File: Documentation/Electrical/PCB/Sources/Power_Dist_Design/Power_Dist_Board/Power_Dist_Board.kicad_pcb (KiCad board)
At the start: 2 copper layers, 145 x 85 mm, 66 parts, among them J1 Battery Connector, J10 GND_Bridge_3, J2 +5V, J3 +5V, J4 +3.3V, J5 +3.3V, J6 GND, J7 GND, J8 GND_Bridge_1, J9 GND_Bridge_2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

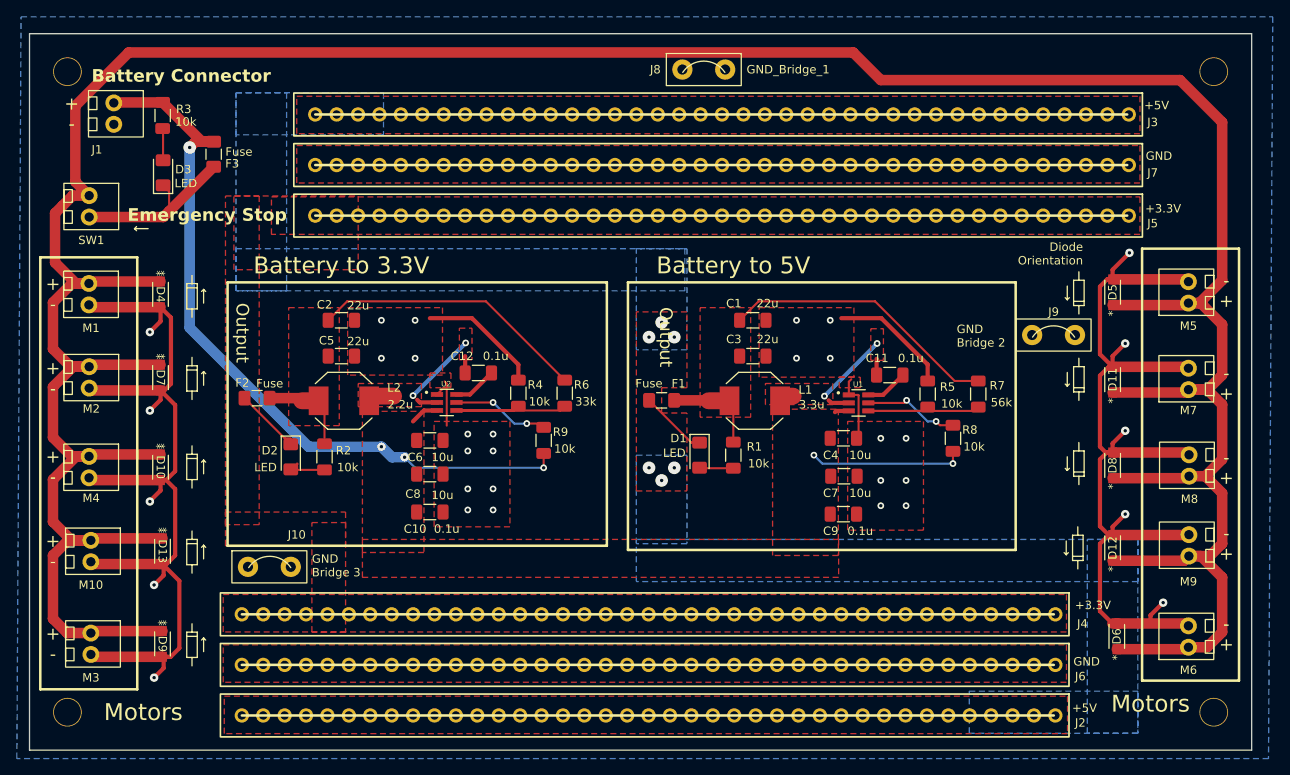
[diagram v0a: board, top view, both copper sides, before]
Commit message: added 3d models to pcb
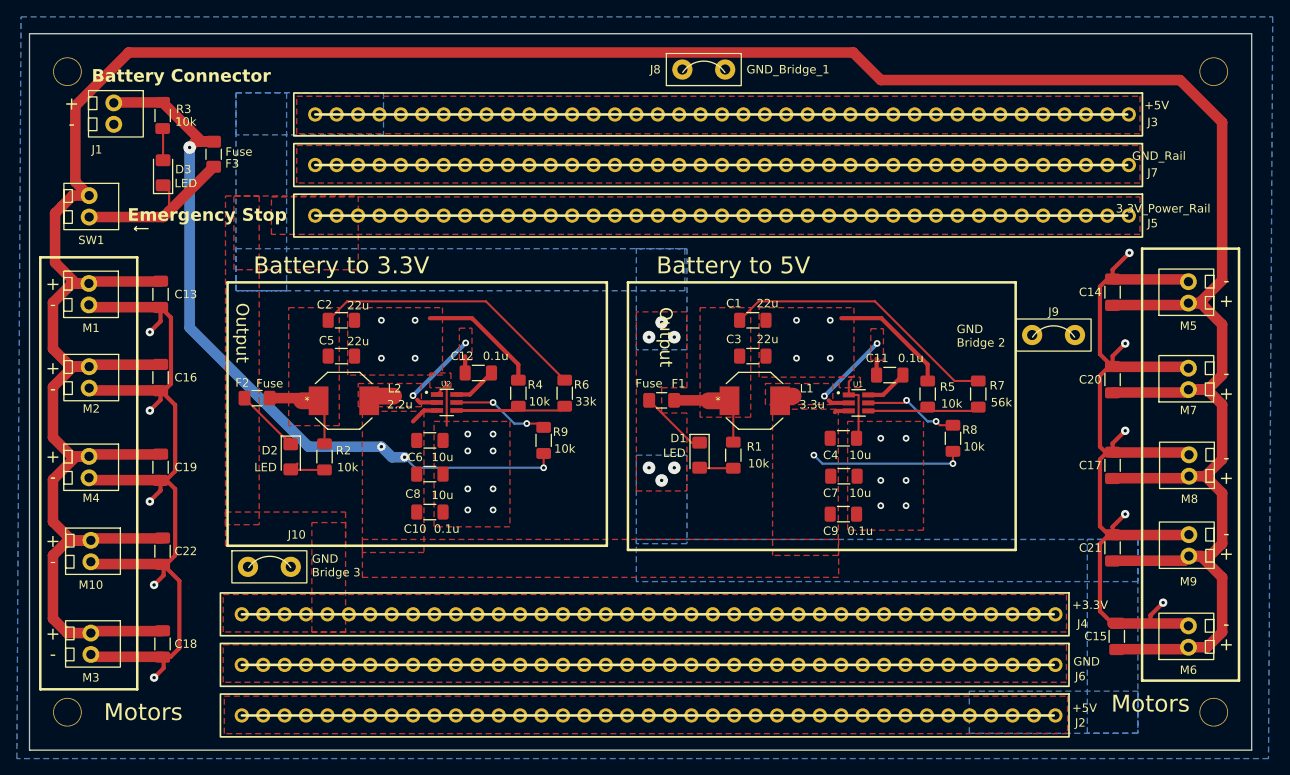
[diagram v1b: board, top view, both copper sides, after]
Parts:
- C13: renamed from D4; value D -> 0.1u; footprint RB070MM:DIO_RB051MM_ROM-M -> Capacitor_SMD:C_1206_3216Metric_Pad1.33x1.80mm_HandSolder
- C14: renamed from D5; value D -> 0.1u; footprint RB070MM:DIO_RB051MM_ROM-M -> Capacitor_SMD:C_1206_3216Metric_Pad1.33x1.80mm_HandSolder
- C15: renamed from D6; value D -> 0.1u; footprint RB070MM:DIO_RB051MM_ROM-M -> Capacitor_SMD:C_1206_3216Metric_Pad1.33x1.80mm_HandSolder
- C16: renamed from D7; value D -> 0.1u; footprint RB070MM:DIO_RB051MM_ROM-M -> Capacitor_SMD:C_1206_3216Metric_Pad1.33x1.80mm_HandSolder
- C17: renamed from D8; value D -> 0.1u; footprint RB070MM:DIO_RB051MM_ROM-M -> Capacitor_SMD:C_1206_3216Metric_Pad1.33x1.80mm_HandSolder
- C18: renamed from D9; value D -> 0.1u; footprint RB070MM:DIO_RB051MM_ROM-M -> Capacitor_SMD:C_1206_3216Metric_Pad1.33x1.80mm_HandSolder
- C19: renamed from D10; value D -> C; footprint RB070MM:DIO_RB051MM_ROM-M -> Capacitor_SMD:C_1206_3216Metric_Pad1.33x1.80mm_HandSolder
- C20: renamed from D11; value D -> 0.1u; footprint RB070MM:DIO_RB051MM_ROM-M -> Capacitor_SMD:C_1206_3216Metric_Pad1.33x1.80mm_HandSolder
- C21: renamed from D12; value D -> 0.1u; footprint RB070MM:DIO_RB051MM_ROM-M -> Capacitor_SMD:C_1206_3216Metric_Pad1.33x1.80mm_HandSolder
- C22: renamed from D13; value D -> 0.1u; footprint RB070MM:DIO_RB051MM_ROM-M -> Capacitor_SMD:C_1206_3216Metric_Pad1.33x1.80mm_HandSolder
- J5: value +3.3V -> 3.3V_Power_Rail
- J7: value GND -> GND_Rail
- L1, L2: footprint L_TDK_SPM6530:IND_SPM6530_TDK -> Power_Dist:IND_SPM6530_TDK
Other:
- board text removed: "Diode Orientation"

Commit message: small changes to power pcb
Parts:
- J5: value 3.3V_Power_Rail -> +3.3V
- J7: value GND_Rail -> GND
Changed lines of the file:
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@@
         (effects (font (size 1 1) (thickness 0.15)))
     )
-    (fp_text value "3.3V_Power_Rail" (at -0.75 -50.26 unlocked) (layer "F.SilkS")
+    (fp_text value "+3.3V" (at -0.75 -50.26 unlocked) (layer "F.SilkS")
         (effects (font (size 1 1) (thickness 0.15)))
     )
@@
         (effects (font (size 1 1) (thickness 0.15)))
     )
-    (fp_text value "GND_Rail" (at -1 -49.76 unlocked) (layer "F.SilkS")
-        (effects (font (size 1 1) (thickness 0.15)))
-    )
+    (fp_text value "GND" (at -1 -49.76 unlocked) (layer "F.SilkS")
+        (effects (font (size 1 1) (thickness 0.15)))
+    )
